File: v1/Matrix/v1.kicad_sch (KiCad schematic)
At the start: 180 parts, among them J1 Conn_01x06, J2 Conn_01x16

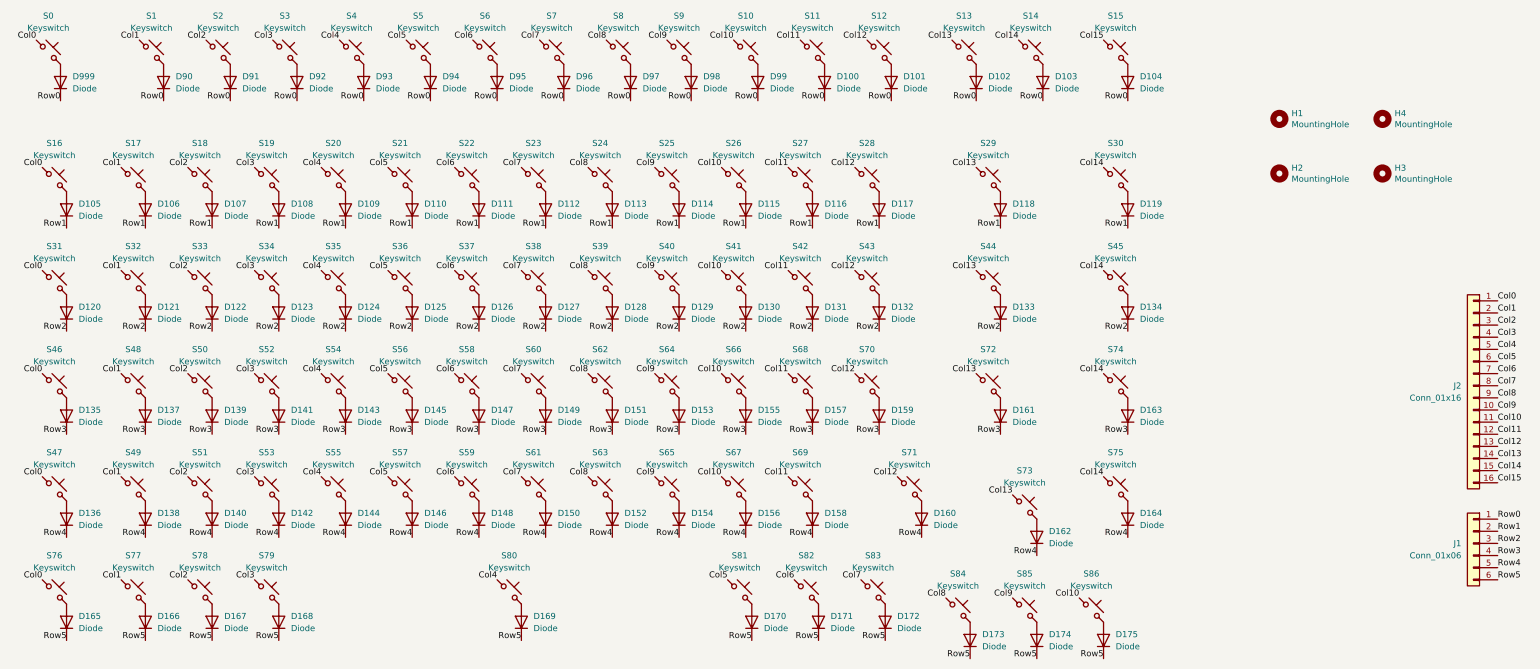
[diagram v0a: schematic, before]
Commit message: additions to the v1 pcb and schematics
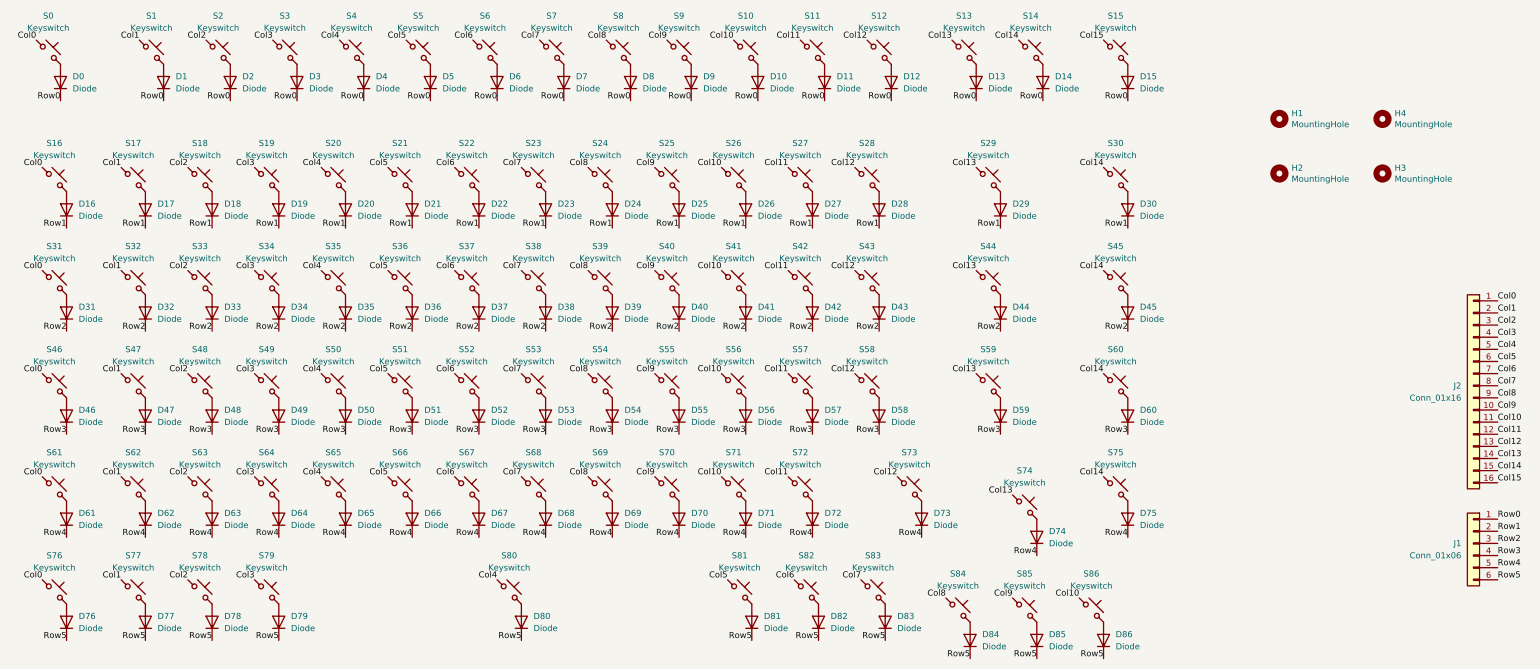
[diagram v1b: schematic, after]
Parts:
- D0: renamed from D999; footprint ScottoKeebs_Components:Diode_SOD-123 -> ScottoKeebs_Components:Diode_DO-35
- D1: renamed from D90; footprint ScottoKeebs_Components:Diode_SOD-123 -> ScottoKeebs_Components:Diode_DO-35
- D10: renamed from D99; footprint ScottoKeebs_Components:Diode_SOD-123 -> ScottoKeebs_Components:Diode_DO-35
- D11: renamed from D100; footprint ScottoKeebs_Components:Diode_SOD-123 -> ScottoKeebs_Components:Diode_DO-35
- D12: renamed from D101; footprint ScottoKeebs_Components:Diode_SOD-123 -> ScottoKeebs_Components:Diode_DO-35
- D13: renamed from D102; footprint ScottoKeebs_Components:Diode_SOD-123 -> ScottoKeebs_Components:Diode_DO-35
- D14: renamed from D103; footprint ScottoKeebs_Components:Diode_SOD-123 -> ScottoKeebs_Components:Diode_DO-35
- D15: renamed from D104; footprint ScottoKeebs_Components:Diode_SOD-123 -> ScottoKeebs_Components:Diode_DO-35
- D16: renamed from D105; footprint ScottoKeebs_Components:Diode_SOD-123 -> ScottoKeebs_Components:Diode_DO-35
- D17: renamed from D106; footprint ScottoKeebs_Components:Diode_SOD-123 -> ScottoKeebs_Components:Diode_DO-35
- D18: renamed from D107; footprint ScottoKeebs_Components:Diode_SOD-123 -> ScottoKeebs_Components:Diode_DO-35
- D19: renamed from D108; footprint ScottoKeebs_Components:Diode_SOD-123 -> ScottoKeebs_Components:Diode_DO-35
- D2: renamed from D91; footprint ScottoKeebs_Components:Diode_SOD-123 -> ScottoKeebs_Components:Diode_DO-35
- D20: renamed from D109; footprint ScottoKeebs_Components:Diode_SOD-123 -> ScottoKeebs_Components:Diode_DO-35
- D21: renamed from D110; footprint ScottoKeebs_Components:Diode_SOD-123 -> ScottoKeebs_Components:Diode_DO-35
- D22: renamed from D111; footprint ScottoKeebs_Components:Diode_SOD-123 -> ScottoKeebs_Components:Diode_DO-35
- D23: renamed from D112; footprint ScottoKeebs_Components:Diode_SOD-123 -> ScottoKeebs_Components:Diode_DO-35
- D24: renamed from D113; footprint ScottoKeebs_Components:Diode_SOD-123 -> ScottoKeebs_Components:Diode_DO-35
- D25: renamed from D114; footprint ScottoKeebs_Components:Diode_SOD-123 -> ScottoKeebs_Components:Diode_DO-35
- D26: renamed from D115; footprint ScottoKeebs_Components:Diode_SOD-123 -> ScottoKeebs_Components:Diode_DO-35
- D27: renamed from D116; footprint ScottoKeebs_Components:Diode_SOD-123 -> ScottoKeebs_Components:Diode_DO-35
- D28: renamed from D117; footprint ScottoKeebs_Components:Diode_SOD-123 -> ScottoKeebs_Components:Diode_DO-35
- D29: renamed from D118; footprint ScottoKeebs_Components:Diode_SOD-123 -> ScottoKeebs_Components:Diode_DO-35
- D3: renamed from D92; footprint ScottoKeebs_Components:Diode_SOD-123 -> ScottoKeebs_Components:Diode_DO-35
- D30: renamed from D119; footprint ScottoKeebs_Components:Diode_SOD-123 -> ScottoKeebs_Components:Diode_DO-35
- D31: renamed from D120; footprint ScottoKeebs_Components:Diode_SOD-123 -> ScottoKeebs_Components:Diode_DO-35
- D32: renamed from D121; footprint ScottoKeebs_Components:Diode_SOD-123 -> ScottoKeebs_Components:Diode_DO-35
- D33: renamed from D122; footprint ScottoKeebs_Components:Diode_SOD-123 -> ScottoKeebs_Components:Diode_DO-35
- D34: renamed from D123; footprint ScottoKeebs_Components:Diode_SOD-123 -> ScottoKeebs_Components:Diode_DO-35
- D35: renamed from D124; footprint ScottoKeebs_Components:Diode_SOD-123 -> ScottoKeebs_Components:Diode_DO-35
- D36: renamed from D125; footprint ScottoKeebs_Components:Diode_SOD-123 -> ScottoKeebs_Components:Diode_DO-35
- D37: renamed from D126; footprint ScottoKeebs_Components:Diode_SOD-123 -> ScottoKeebs_Components:Diode_DO-35
- D38: renamed from D127; footprint ScottoKeebs_Components:Diode_SOD-123 -> ScottoKeebs_Components:Diode_DO-35
- D39: renamed from D128; footprint ScottoKeebs_Components:Diode_SOD-123 -> ScottoKeebs_Components:Diode_DO-35
- D4: renamed from D93; footprint ScottoKeebs_Components:Diode_SOD-123 -> ScottoKeebs_Components:Diode_DO-35
- D40: renamed from D129; footprint ScottoKeebs_Components:Diode_SOD-123 -> ScottoKeebs_Components:Diode_DO-35
- D41: renamed from D130; footprint ScottoKeebs_Components:Diode_SOD-123 -> ScottoKeebs_Components:Diode_DO-35
- D42: renamed from D131; footprint ScottoKeebs_Components:Diode_SOD-123 -> ScottoKeebs_Components:Diode_DO-35
- D43: renamed from D132; footprint ScottoKeebs_Components:Diode_SOD-123 -> ScottoKeebs_Components:Diode_DO-35
- D44: renamed from D133; footprint ScottoKeebs_Components:Diode_SOD-123 -> ScottoKeebs_Components:Diode_DO-35
- D45: renamed from D134; footprint ScottoKeebs_Components:Diode_SOD-123 -> ScottoKeebs_Components:Diode_DO-35
- D46: renamed from D135; footprint ScottoKeebs_Components:Diode_SOD-123 -> ScottoKeebs_Components:Diode_DO-35
- D47: renamed from D137; footprint ScottoKeebs_Components:Diode_SOD-123 -> ScottoKeebs_Components:Diode_DO-35
- D48: renamed from D139; footprint ScottoKeebs_Components:Diode_SOD-123 -> ScottoKeebs_Components:Diode_DO-35
- D49: renamed from D141; footprint ScottoKeebs_Components:Diode_SOD-123 -> ScottoKeebs_Components:Diode_DO-35
- D5: renamed from D94; footprint ScottoKeebs_Components:Diode_SOD-123 -> ScottoKeebs_Components:Diode_DO-35
- D50: renamed from D143; footprint ScottoKeebs_Components:Diode_SOD-123 -> ScottoKeebs_Components:Diode_DO-35
- D51: renamed from D145; footprint ScottoKeebs_Components:Diode_SOD-123 -> ScottoKeebs_Components:Diode_DO-35
- D52: renamed from D147; footprint ScottoKeebs_Components:Diode_SOD-123 -> ScottoKeebs_Components:Diode_DO-35
- D53: renamed from D149; footprint ScottoKeebs_Components:Diode_SOD-123 -> ScottoKeebs_Components:Diode_DO-35
- D54: renamed from D151; footprint ScottoKeebs_Components:Diode_SOD-123 -> ScottoKeebs_Components:Diode_DO-35
- D55: renamed from D153; footprint ScottoKeebs_Components:Diode_SOD-123 -> ScottoKeebs_Components:Diode_DO-35
- D56: renamed from D155; footprint ScottoKeebs_Components:Diode_SOD-123 -> ScottoKeebs_Components:Diode_DO-35
- D57: renamed from D157; footprint ScottoKeebs_Components:Diode_SOD-123 -> ScottoKeebs_Components:Diode_DO-35
- D58: renamed from D159; footprint ScottoKeebs_Components:Diode_SOD-123 -> ScottoKeebs_Components:Diode_DO-35
- D59: renamed from D161; footprint ScottoKeebs_Components:Diode_SOD-123 -> ScottoKeebs_Components:Diode_DO-35
- D6: renamed from D95; footprint ScottoKeebs_Components:Diode_SOD-123 -> ScottoKeebs_Components:Diode_DO-35
- D60: renamed from D163; footprint ScottoKeebs_Components:Diode_SOD-123 -> ScottoKeebs_Components:Diode_DO-35
- D61: renamed from D136; footprint ScottoKeebs_Components:Diode_SOD-123 -> ScottoKeebs_Components:Diode_DO-35
- D62: renamed from D138; footprint ScottoKeebs_Components:Diode_SOD-123 -> ScottoKeebs_Components:Diode_DO-35
- D63: renamed from D140; footprint ScottoKeebs_Components:Diode_SOD-123 -> ScottoKeebs_Components:Diode_DO-35
- D64: renamed from D142; footprint ScottoKeebs_Components:Diode_SOD-123 -> ScottoKeebs_Components:Diode_DO-35
- D65: renamed from D144; footprint ScottoKeebs_Components:Diode_SOD-123 -> ScottoKeebs_Components:Diode_DO-35
- D66: renamed from D146; footprint ScottoKeebs_Components:Diode_SOD-123 -> ScottoKeebs_Components:Diode_DO-35
- D67: renamed from D148; footprint ScottoKeebs_Components:Diode_SOD-123 -> ScottoKeebs_Components:Diode_DO-35
- D68: renamed from D150; footprint ScottoKeebs_Components:Diode_SOD-123 -> ScottoKeebs_Components:Diode_DO-35
- D69: renamed from D152; footprint ScottoKeebs_Components:Diode_SOD-123 -> ScottoKeebs_Components:Diode_DO-35
- D7: renamed from D96; footprint ScottoKeebs_Components:Diode_SOD-123 -> ScottoKeebs_Components:Diode_DO-35
- D70: renamed from D154; footprint ScottoKeebs_Components:Diode_SOD-123 -> ScottoKeebs_Components:Diode_DO-35
- D71: renamed from D156; footprint ScottoKeebs_Components:Diode_SOD-123 -> ScottoKeebs_Components:Diode_DO-35
- D72: renamed from D158; footprint ScottoKeebs_Components:Diode_SOD-123 -> ScottoKeebs_Components:Diode_DO-35
- D73: renamed from D160; footprint ScottoKeebs_Components:Diode_SOD-123 -> ScottoKeebs_Components:Diode_DO-35
- D74: renamed from D162; footprint ScottoKeebs_Components:Diode_SOD-123 -> ScottoKeebs_Components:Diode_DO-35
- D75: renamed from D164; footprint ScottoKeebs_Components:Diode_SOD-123 -> ScottoKeebs_Components:Diode_DO-35
- D76: renamed from D165; footprint ScottoKeebs_Components:Diode_SOD-123 -> ScottoKeebs_Components:Diode_DO-35
- D77: renamed from D166; footprint ScottoKeebs_Components:Diode_SOD-123 -> ScottoKeebs_Components:Diode_DO-35
- D78: renamed from D167; footprint ScottoKeebs_Components:Diode_SOD-123 -> ScottoKeebs_Components:Diode_DO-35
- D79: renamed from D168; footprint ScottoKeebs_Components:Diode_SOD-123 -> ScottoKeebs_Components:Diode_DO-35
- D8: renamed from D97; footprint ScottoKeebs_Components:Diode_SOD-123 -> ScottoKeebs_Components:Diode_DO-35
- D80: renamed from D169; footprint ScottoKeebs_Components:Diode_SOD-123 -> ScottoKeebs_Components:Diode_DO-35
- D81: renamed from D170; footprint ScottoKeebs_Components:Diode_SOD-123 -> ScottoKeebs_Components:Diode_DO-35
- D82: renamed from D171; footprint ScottoKeebs_Components:Diode_SOD-123 -> ScottoKeebs_Components:Diode_DO-35
- D83: renamed from D172; footprint ScottoKeebs_Components:Diode_SOD-123 -> ScottoKeebs_Components:Diode_DO-35
- D84: renamed from D173; footprint ScottoKeebs_Components:Diode_SOD-123 -> ScottoKeebs_Components:Diode_DO-35
- D85: renamed from D174; footprint ScottoKeebs_Components:Diode_SOD-123 -> ScottoKeebs_Components:Diode_DO-35
- D86: renamed from D175; footprint ScottoKeebs_Components:Diode_SOD-123 -> ScottoKeebs_Components:Diode_DO-35
- D9: renamed from D98; footprint ScottoKeebs_Components:Diode_SOD-123 -> ScottoKeebs_Components:Diode_DO-35
- renumbered S48 to S47, S50 to S48, S52 to S49, S54 to S50, S56 to S51, S58 to S52, S60 to S53, S62 to S54, S64 to S55, S66 to S56, S68 to S57, S70 to S58, S72 to S59, S74 to S60, S47 to S61, S49 to S62, S51 to S63, S53 to S64, S55 to S65, S57 to S66, S59 to S67, S61 to S68, S63 to S69, S65 to S70, S67 to S71, S69 to S72, S71 to S73, S73 to S74
